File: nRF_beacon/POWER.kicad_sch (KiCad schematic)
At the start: 15 parts, among them U2 NPM1300-QEAA-R7

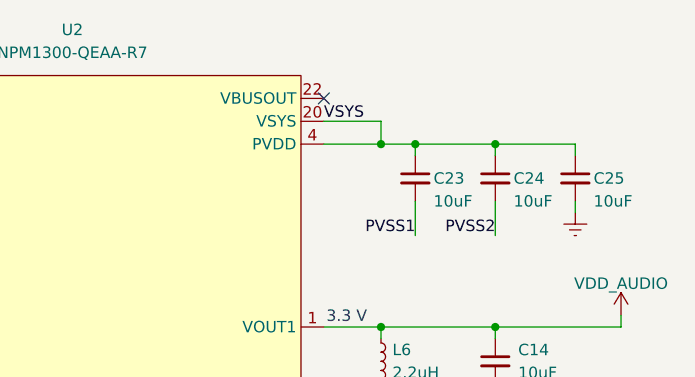
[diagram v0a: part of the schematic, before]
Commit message: Adjustments to GPIO connector. Added testpads. Polygon pour by antenna for correct impedance matching
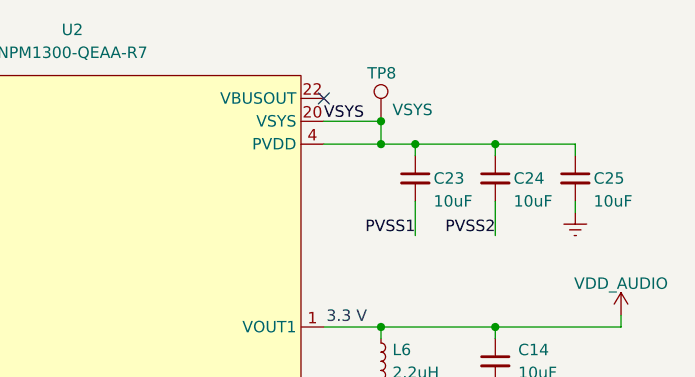
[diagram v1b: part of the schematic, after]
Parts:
- added TP8: VSYS, TestPoint:TestPoint_Pad_D1.0mm, symbol Connector:TestPoint
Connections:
- net VSYS: now also TP8.1
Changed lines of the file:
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@@
+		(color 0 0 0 0)
+	)
+	(junction
+		(at 182.88 60.96)
+		(diameter 0)
 		(color 0 0 0 0)
 	)
@@
 					(unit 1)
 				)
+			)
+		)
+	)
+	(symbol
+		(lib_id "Connector:TestPoint")
+		(at 182.88 60.96 0)
+		(unit 1)
+		(exclude_from_sim no)
+		(in_bom yes)
+		(on_board yes)
+		(dnp no)
+		(property "Reference" "TP8"
+			(at 181.356 55.626 0)
+			(effects
+				(font
+					(size 1.27 1.27)
+				)
+				(justify left)
+			)
+		)
+		(property "Value" "VSYS"
+			(at 184.15 59.69 0)
+			(effects
+				(font
+					(size 1.27 1.27)
+				)
+				(justify left)
+			)
+		)
+		(property "Footprint" "TestPoint:TestPoint_Pad_D1.0mm"
+			(at 187.96 60.96 0)
+			(effects
+				(font
+					(size 1.27 1.27)
+				)
+				(hide yes)
+			)
+		)
+		(property "Datasheet" "~"
+			(at 187.96 60.96 0)
+			(effects
+				(font
+					(size 1.27 1.27)
+				)
+				(hide yes)
+			)
+		)
+		(property "Description" "test point"
+			(at 182.88 60.96 0)
+			(effects
+				(font
+					(size 1.27 1.27)
+				)
+				(hide yes)
+			)
+		)
+		(pin "1"
+		)
+		(instances
+			(project ""
+				(path "/1290e5f5-b91f-4d6e-b440-6b78e8fdc212/1b7d8d32-f2af-4099-9901-f3134d87cd68"
+					(reference "TP8")
+					(unit 1)
+				)

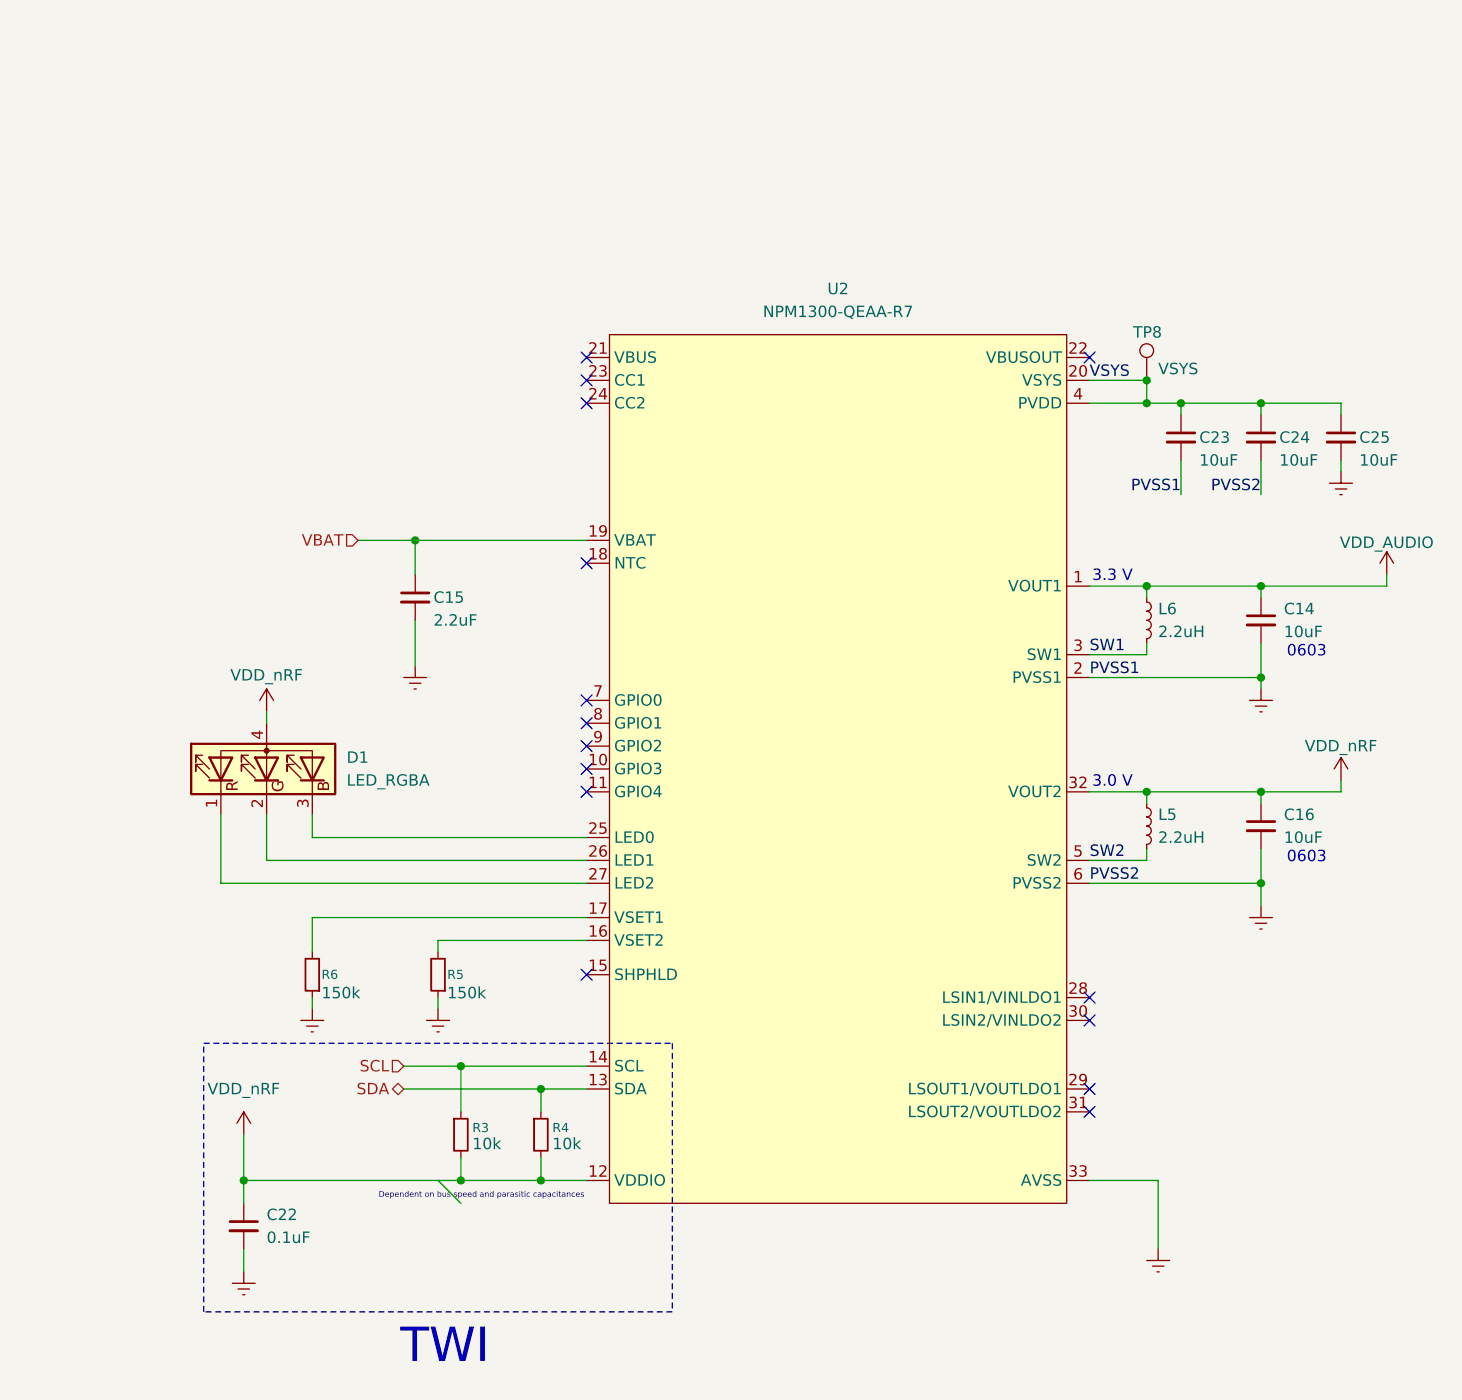
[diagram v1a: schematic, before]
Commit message: Added stitching vias and completed DRC tests
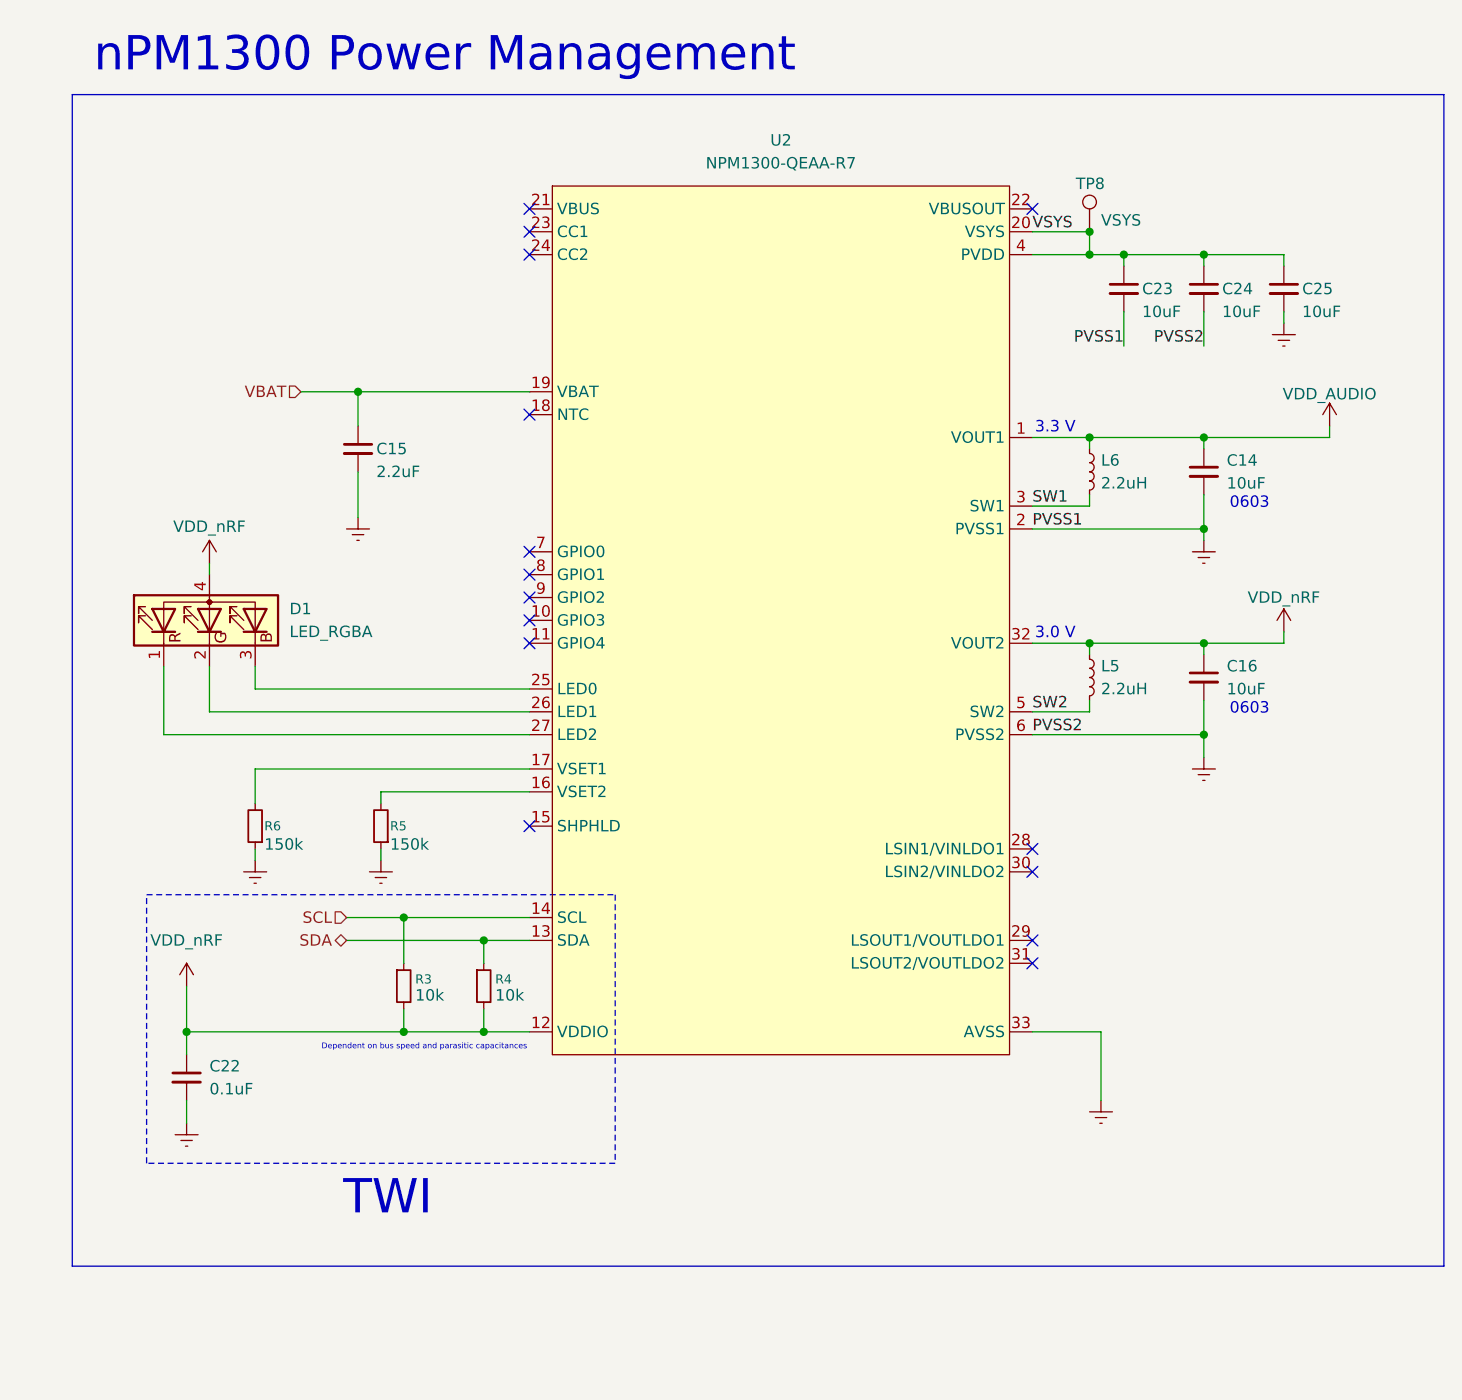
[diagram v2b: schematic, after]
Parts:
- C14, C16: MPN (none) -> KGM15CR51E106KT; Price (none) -> 5.09
- R3, R4: MPN (none) -> CRCW040210K0FHEDP; Price (none) -> 3.19
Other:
- note added: "nPM1300 Power Management"
- company: (none) -> Mathias Ekse
- title: (none) -> Power Management (nPM1300)
- moved on the sheet: C14, C15, C16, C22, C23, C24, C25, D1, L5, L6, R3, R4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
